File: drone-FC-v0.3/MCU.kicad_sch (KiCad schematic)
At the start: 1 part, among them U2 ESP32-S3-WROOM-1

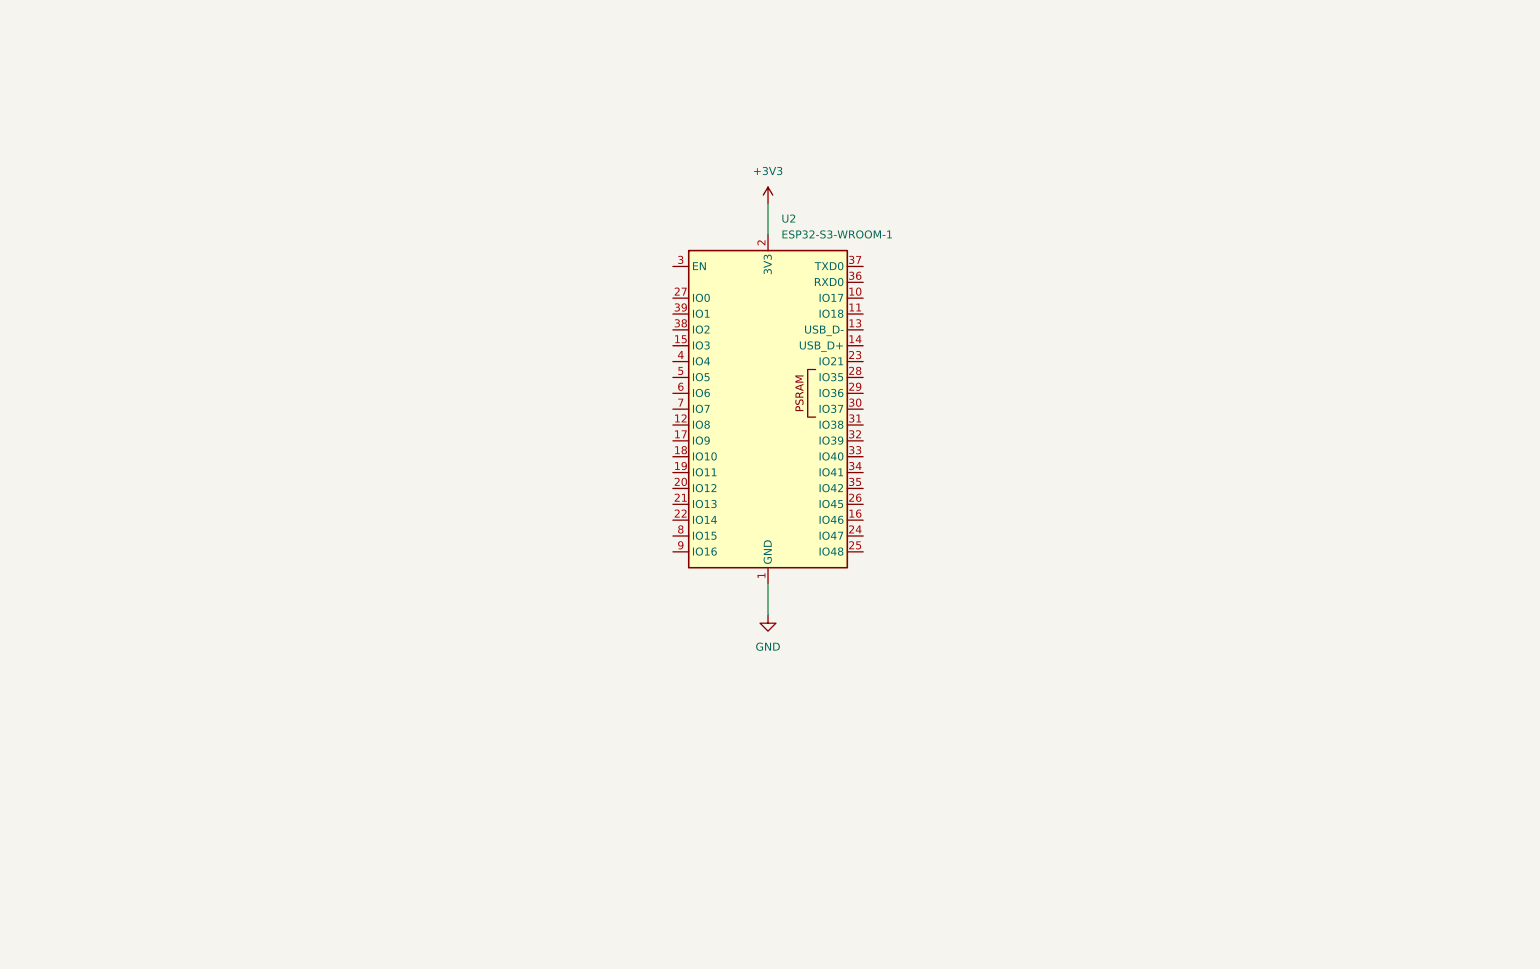
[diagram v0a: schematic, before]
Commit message: what
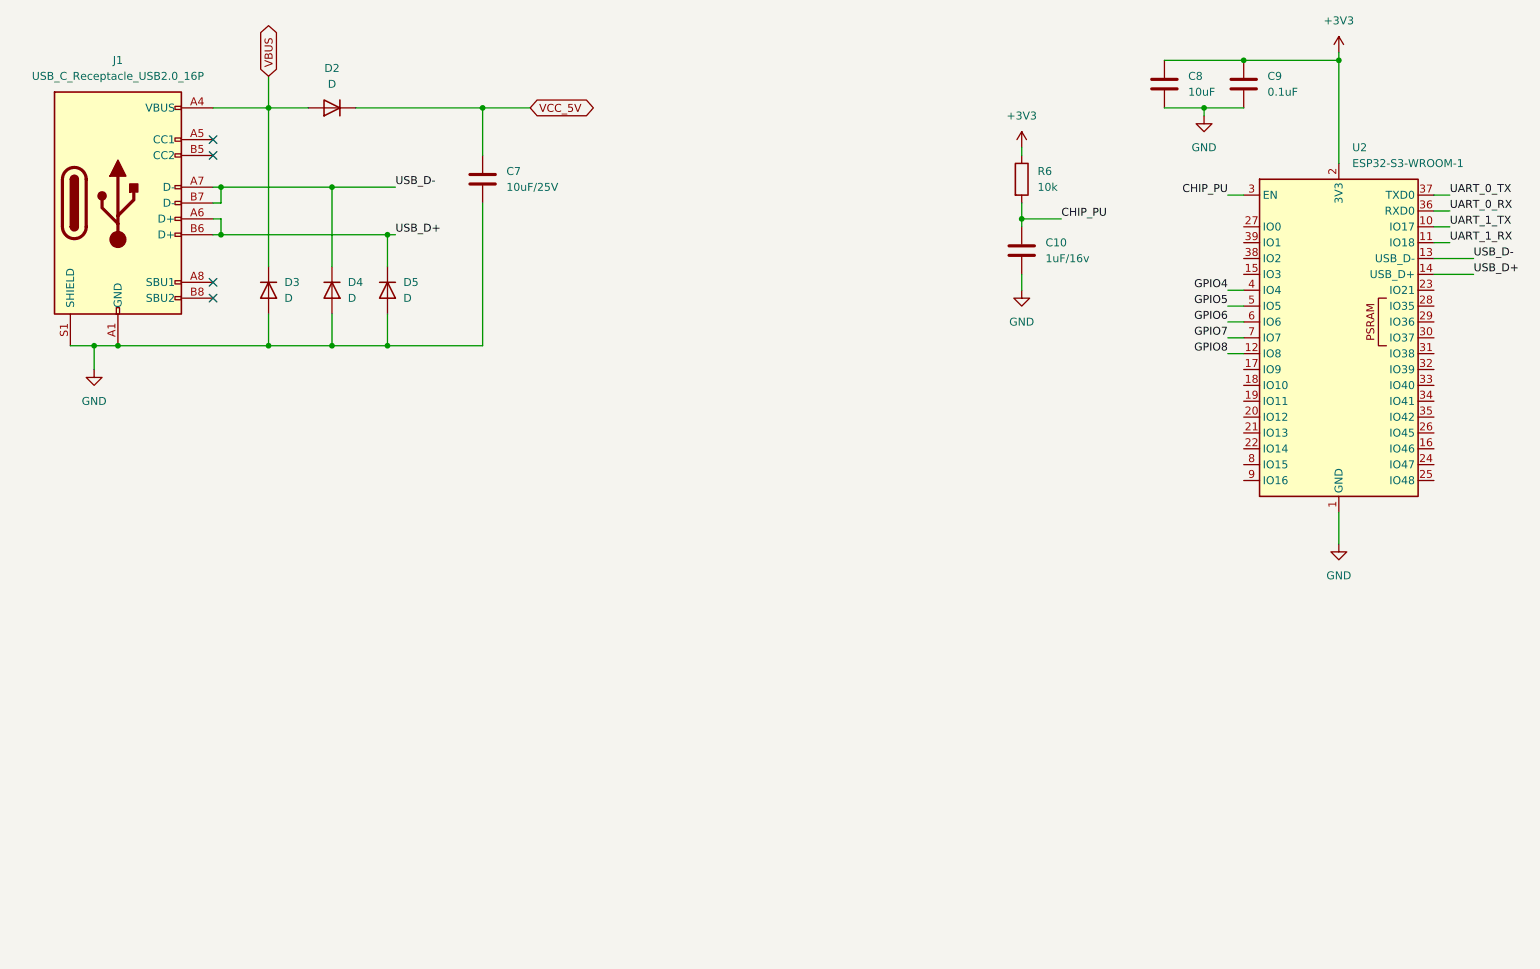
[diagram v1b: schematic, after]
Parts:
- added C10: 1uF/16v, Capacitor_SMD:C_0603_1608Metric, symbol Device:C
- added C7: 10uF/25V, Capacitor_SMD:C_0603_1608Metric, symbol Device:C
- added C8: 10uF, Capacitor_SMD:C_0603_1608Metric, symbol Device:C
- added C9: 0.1uF, Capacitor_SMD:C_0603_1608Metric, symbol Device:C
- added D2: D, Diode_SMD:D_SOD-123F, symbol Device:D
- added D3, D4, D5: D, Diode_SMD:D_SOD-523, symbol Device:D
- added J1: USB_C_Receptacle_USB2.0_16P, Connector_USB:USB_C_Receptacle_GCT_USB4105-xx-A_16P_TopMnt_Horizontal, symbol Connector:USB_C_Receptacle_USB2.0_16P
- added R6: 10k, Resistor_SMD:R_0603_1608Metric, symbol Device:R
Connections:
- net +3V3: now also C8.1, C9.1, R6.1
- net GND: now also C10.2, C7.2, C8.2, C9.2, D3.2 (A), D4.2 (A), D5.2 (A), J1.A1 (GND), J1.A12 (GND), J1.B1 (GND), J1.B12 (GND), J1.S1 (SHIELD)
- net UART_1_TX: now reaches U2.10 (IO17)
- net UART_1_RX: now reaches U2.11 (IO18)
- net GPIO8: now reaches U2.12 (IO8)
- net USB_D-: now reaches U2.13 (USB_D-)
- net USB_D-: now also D4.1 (K), J1.A7 (D-), J1.B7 (D-)
- net USB_D+: now reaches U2.14 (USB_D+)
- net USB_D+: now also D5.1 (K), J1.A6 (D+), J1.B6 (D+)
- net CHIP_PU: now reaches U2.3 (EN)
- net CHIP_PU: now also C10.1, R6.2
- net UART_0_RX: now reaches U2.36 (RXD0)
- net UART_0_TX: now reaches U2.37 (TXD0)
- net GPIO4: now reaches U2.4 (IO4)
- net GPIO5: now reaches U2.5 (IO5)
- net GPIO6: now reaches U2.6 (IO6)
- net GPIO7: now reaches U2.7 (IO7)
- new net VBUS: D2.2 (A), D3.1 (K), J1.A4 (VBUS), J1.A9 (VBUS), J1.B4 (VBUS), J1.B9 (VBUS)
- new net VCC_5V: C7.1, D2.1 (K)
- no-connect marks 0 -> 4
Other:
- moved on the sheet: U2

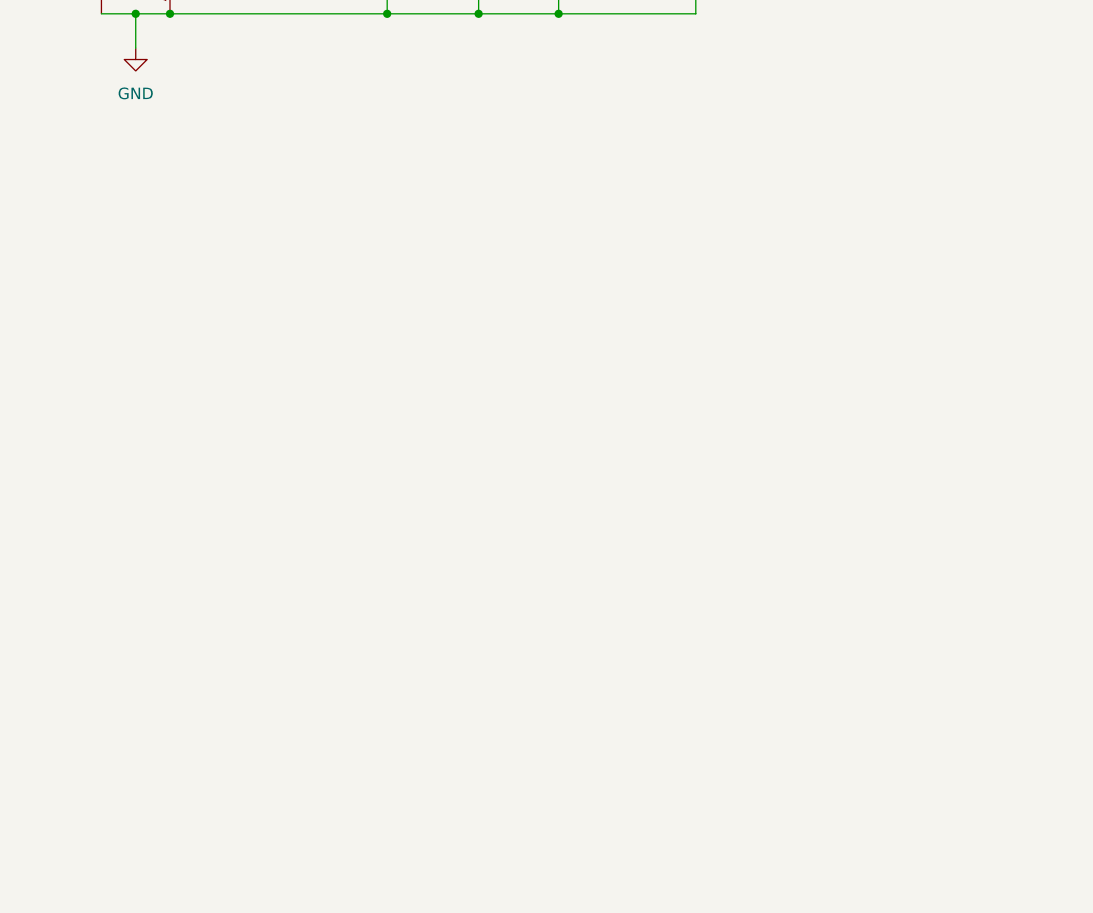
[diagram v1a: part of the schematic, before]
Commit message: added USBC and IMU sensor
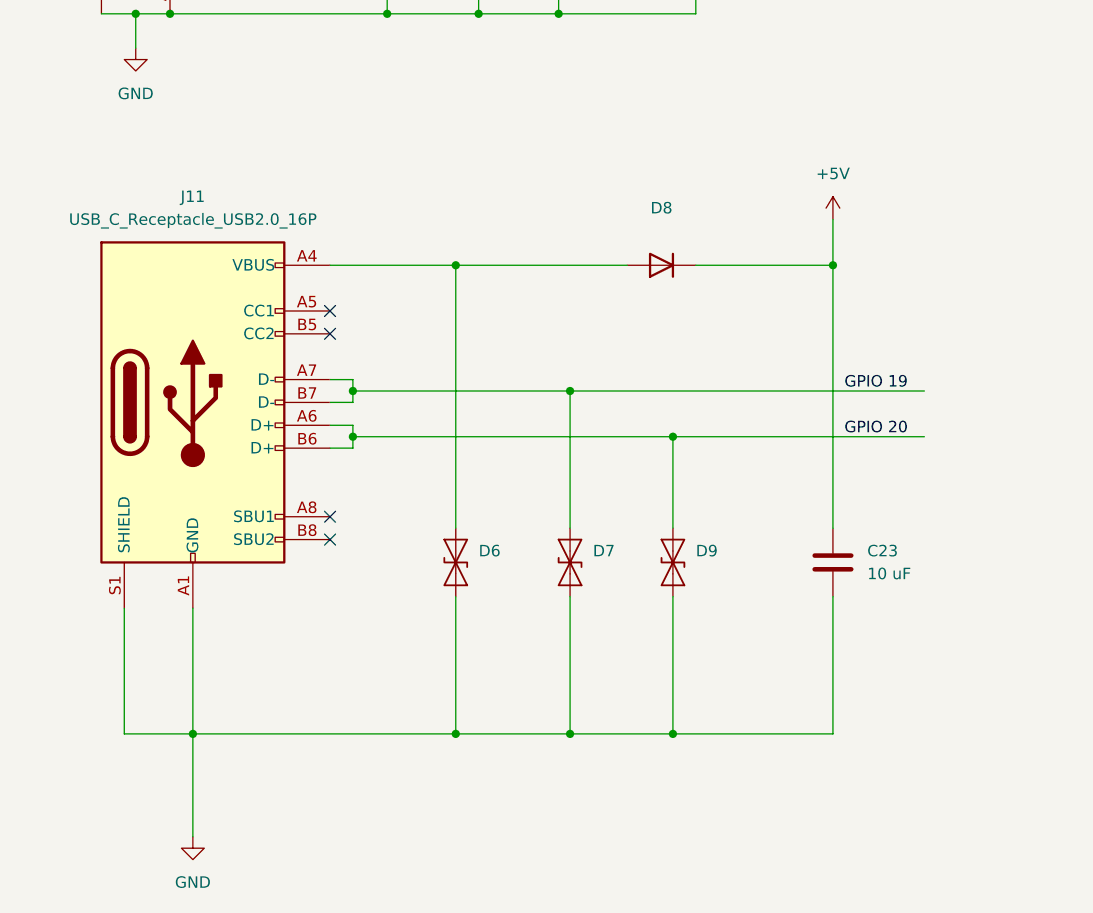
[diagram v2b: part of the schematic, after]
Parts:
- added C23: 10 uF, Capacitor_SMD:C_0201_0603Metric, symbol Device:C
- added D6, D7, D9: ESD9B3.3ST5G, Diode_SMD:D_SOD-923, symbol Diode:ESD9B3.3ST5G
- added D8: 1N4148WT, Diode_SMD:D_SOD-523, symbol Diode:1N4148WT
- added J11: USB_C_Receptacle_USB2.0_16P, Connector_USB:USB_C_Receptacle_Amphenol_124019772112A, symbol Connector:USB_C_Receptacle_USB2.0_16P
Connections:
- net GND: now also C23.2, D6.1 (A1), D7.1 (A1), D9.1 (A1), J11.A1 (GND), J11.A12 (GND), J11.B1 (GND), J11.B12 (GND), J11.S1 (SHIELD)
- new net: D6.2 (A2), D8.2 (A), J11.A4 (VBUS), J11.A9 (VBUS), J11.B4 (VBUS), J11.B9 (VBUS)
- new net +5V: C23.1, D8.1 (K)
- new net GPIO 19: D7.2 (A2), J11.A7 (D-), J11.B7 (D-)
- new net GPIO 20: D9.2 (A2), J11.A6 (D+), J11.B6 (D+)
- no-connect marks 4 -> 8

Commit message: added sensor connections
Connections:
- net SCLK: now reaches U2.15 (IO3)
- net Low_chip_selected: now reaches U2.17 (IO9)
- net SCL_MAG: now reaches U2.18 (IO10)
- net SDA_MAG: now reaches U2.19 (IO11)
- net SDO1: now reaches U2.30 (IO37)
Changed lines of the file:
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@@
+	(wire
+		(pts
+			(xy 200.66 73.66) (xy 210.82 73.66)
+		)
+		(stroke
+			(width 0)
+			(type default)
+		)
+	)
 	(wire
 		(pts
@@
 	(wire
 		(pts
+			(xy 203.2 55.88) (xy 210.82 55.88)
+		)
+		(stroke
+			(width 0)
+			(type default)
+		)
+	)
+	(wire
+		(pts
 			(xy 88.9 29.21) (xy 96.52 29.21)
 		)
@@
 	(wire
 		(pts
+			(xy 193.04 71.12) (xy 210.82 71.12)
+		)
+		(stroke
+			(width 0)
+			(type default)
+		)
+	)
+	(wire
+		(pts
+			(xy 200.66 76.2) (xy 210.82 76.2)
+		)
+		(stroke
+			(width 0)
+			(type default)
+		)
+	)
+	(wire
+		(pts
 			(xy 241.3 45.72) (xy 243.84 45.72)
 		)
@@
 			(width 0)
 			(type default)
+		)
+	)
+	(label "Low_chip_selected"
+		(at 193.04 71.12 0)
+		(effects
+			(font
+				(size 1.27 1.27)
+			)
+			(justify left bottom)
 		)
 	)
@@
 		)
 	)
+	(label "SCLK"
+		(at 203.2 55.88 0)
+		(effects
+			(font
+				(size 1.27 1.27)
+			)
+			(justify left bottom)
+		)
+	)
 	(label "CHIP_PU"
 		(at 181.61 46.99 0)
@@
 		)
 	)
+	(label "SCL_MAG"
+		(at 200.66 73.66 0)
+		(effects
+			(font
+				(size 1.27 1.27)
+			)
+			(justify left bottom)
+		)
+	)
 	(label "USB_D-"
 		(at 74.93 41.91 0)
@@
 		)
 	)
+	(label "SDA_MAG"
+		(at 200.66 76.2 0)
+		(effects
+			(font
+				(size 1.27 1.27)
+			)
+			(justify left bottom)
+		)
+	)
 	(label "GPIO6"
 		(at 208.28 63.5 180)
@@
 		)
 	)
+	(label "SDO1"
+		(at 241.3 66.04 0)
+		(effects
+			(font
+				(size 1.27 1.27)
+			)
+			(justify left bottom)
+		)
+	)

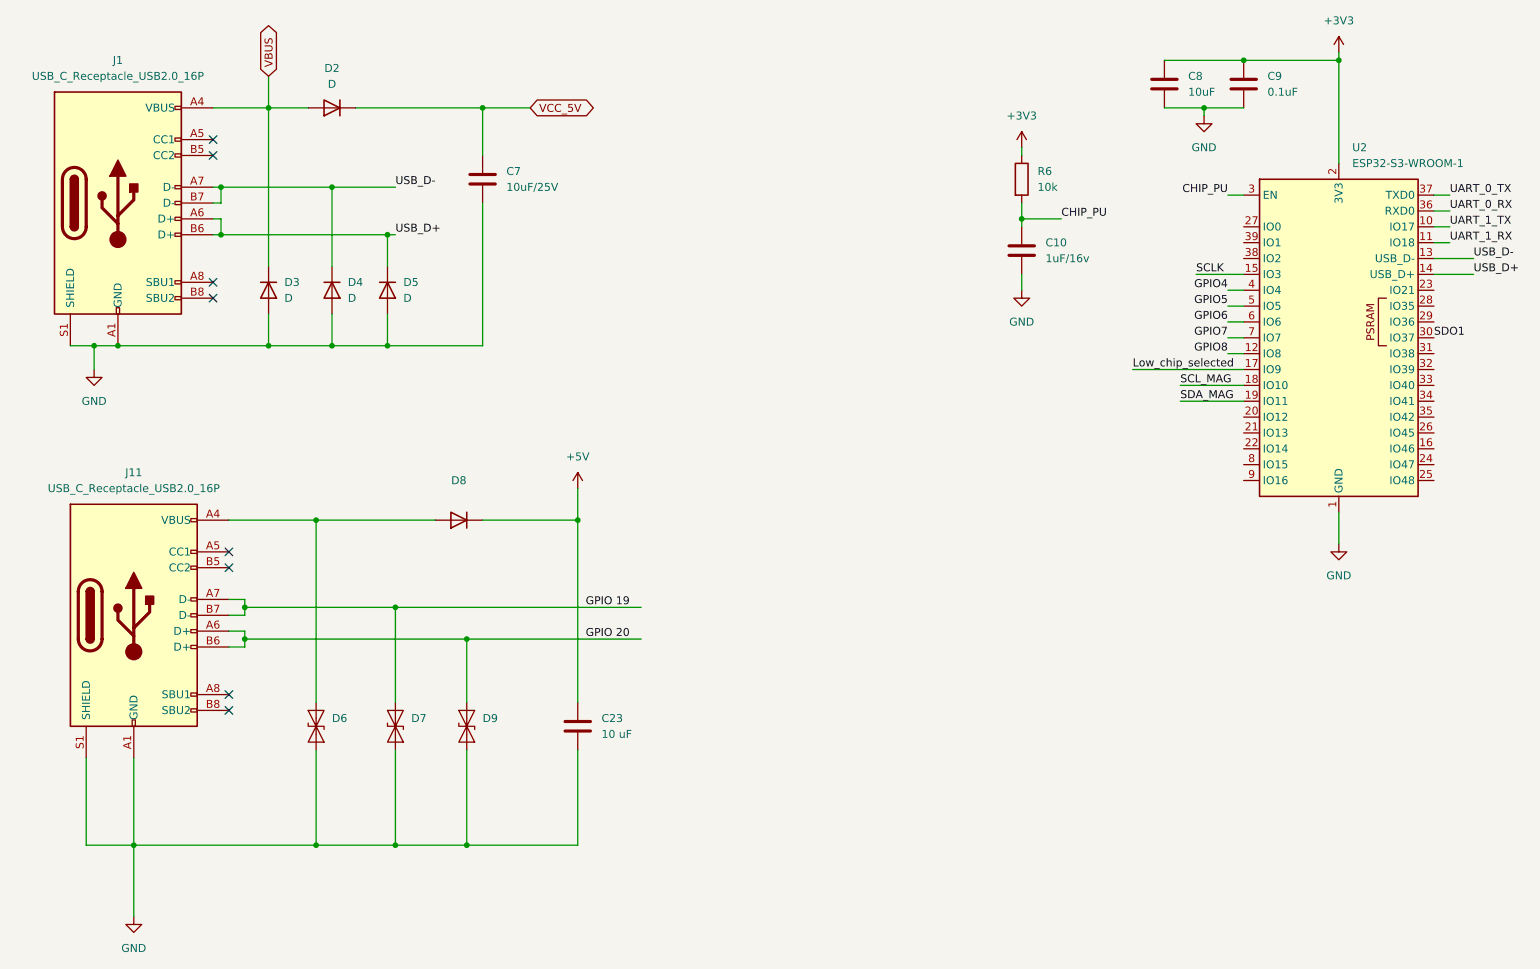
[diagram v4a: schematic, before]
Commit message: added bmi088
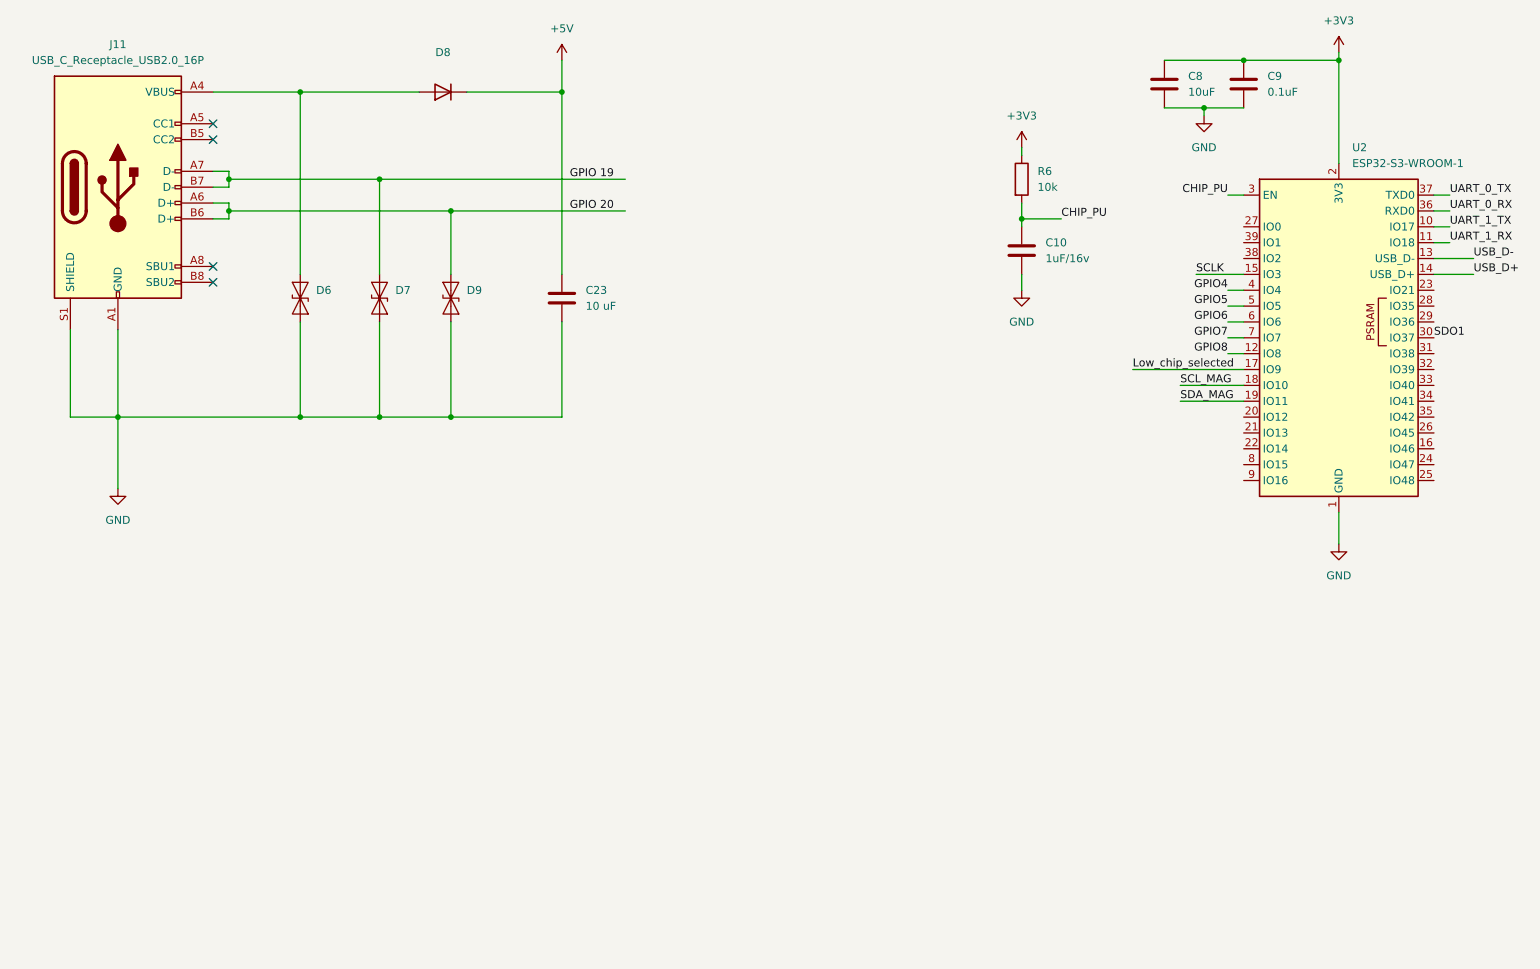
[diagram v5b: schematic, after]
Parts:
- removed C7: 10uF/25V, Capacitor_SMD:C_0603_1608Metric, symbol Device:C
- removed D2: D, Diode_SMD:D_SOD-123F, symbol Device:D
- removed D3, D4, D5: D, Diode_SMD:D_SOD-523, symbol Device:D
- removed J1: USB_C_Receptacle_USB2.0_16P, Connector_USB:USB_C_Receptacle_GCT_USB4105-xx-A_16P_TopMnt_Horizontal, symbol Connector:USB_C_Receptacle_USB2.0_16P
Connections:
- no-connect marks 8 -> 4
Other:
- moved on the sheet: C23, D6, D7, D8, D9, J11

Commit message: modified the schematics to three sensors and added some of the PCB layouts
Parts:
- J11: footprint Connector_USB:USB_C_Receptacle_Amphenol_124019772112A -> Connector_USB:USB_C_Receptacle_Palconn_UTC16-G
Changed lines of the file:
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@@
 			)
 		)
-		(property "Footprint" "Connector_USB:USB_C_Receptacle_Amphenol_124019772112A"
+		(property "Footprint" "Connector_USB:USB_C_Receptacle_Palconn_UTC16-G"
 			(at 34.29 41.91 0)
 			(hide yes)

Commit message: fixed usb footprint issue
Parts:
- J11: footprint Connector_USB:USB_C_Receptacle_Palconn_UTC16-G -> Connector_USB:USB_C_Receptacle_HRO_TYPE-C-31-M-12
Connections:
- net GND: no longer J11.S1 (SHIELD)
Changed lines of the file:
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@@
-	(wire
-		(pts
-			(xy 22.86 78.74) (xy 30.48 78.74)
-		)
-		(stroke
-			(width 0)
-			(type default)
-		)
-	)
 	(wire
 		(pts
@@
 		(pts
 			(xy 72.39 40.64) (xy 72.39 55.88)
-		)
-		(stroke
-			(width 0)
-			(type default)
-		)
-	)
-	(wire
-		(pts
-			(xy 22.86 64.77) (xy 22.86 78.74)
 		)
 		(stroke
@@
 			)
 		)
-		(property "Footprint" "Connector_USB:USB_C_Receptacle_Palconn_UTC16-G"
+		(property "Footprint" "Connector_USB:USB_C_Receptacle_HRO_TYPE-C-31-M-12"
 			(at 34.29 41.91 0)
 			(hide yes)
@@
 		(pin "A1"
 		)
-		(pin "S1"
-		)
 		(pin "A12"
